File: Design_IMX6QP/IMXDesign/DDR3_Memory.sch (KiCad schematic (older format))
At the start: 0 parts

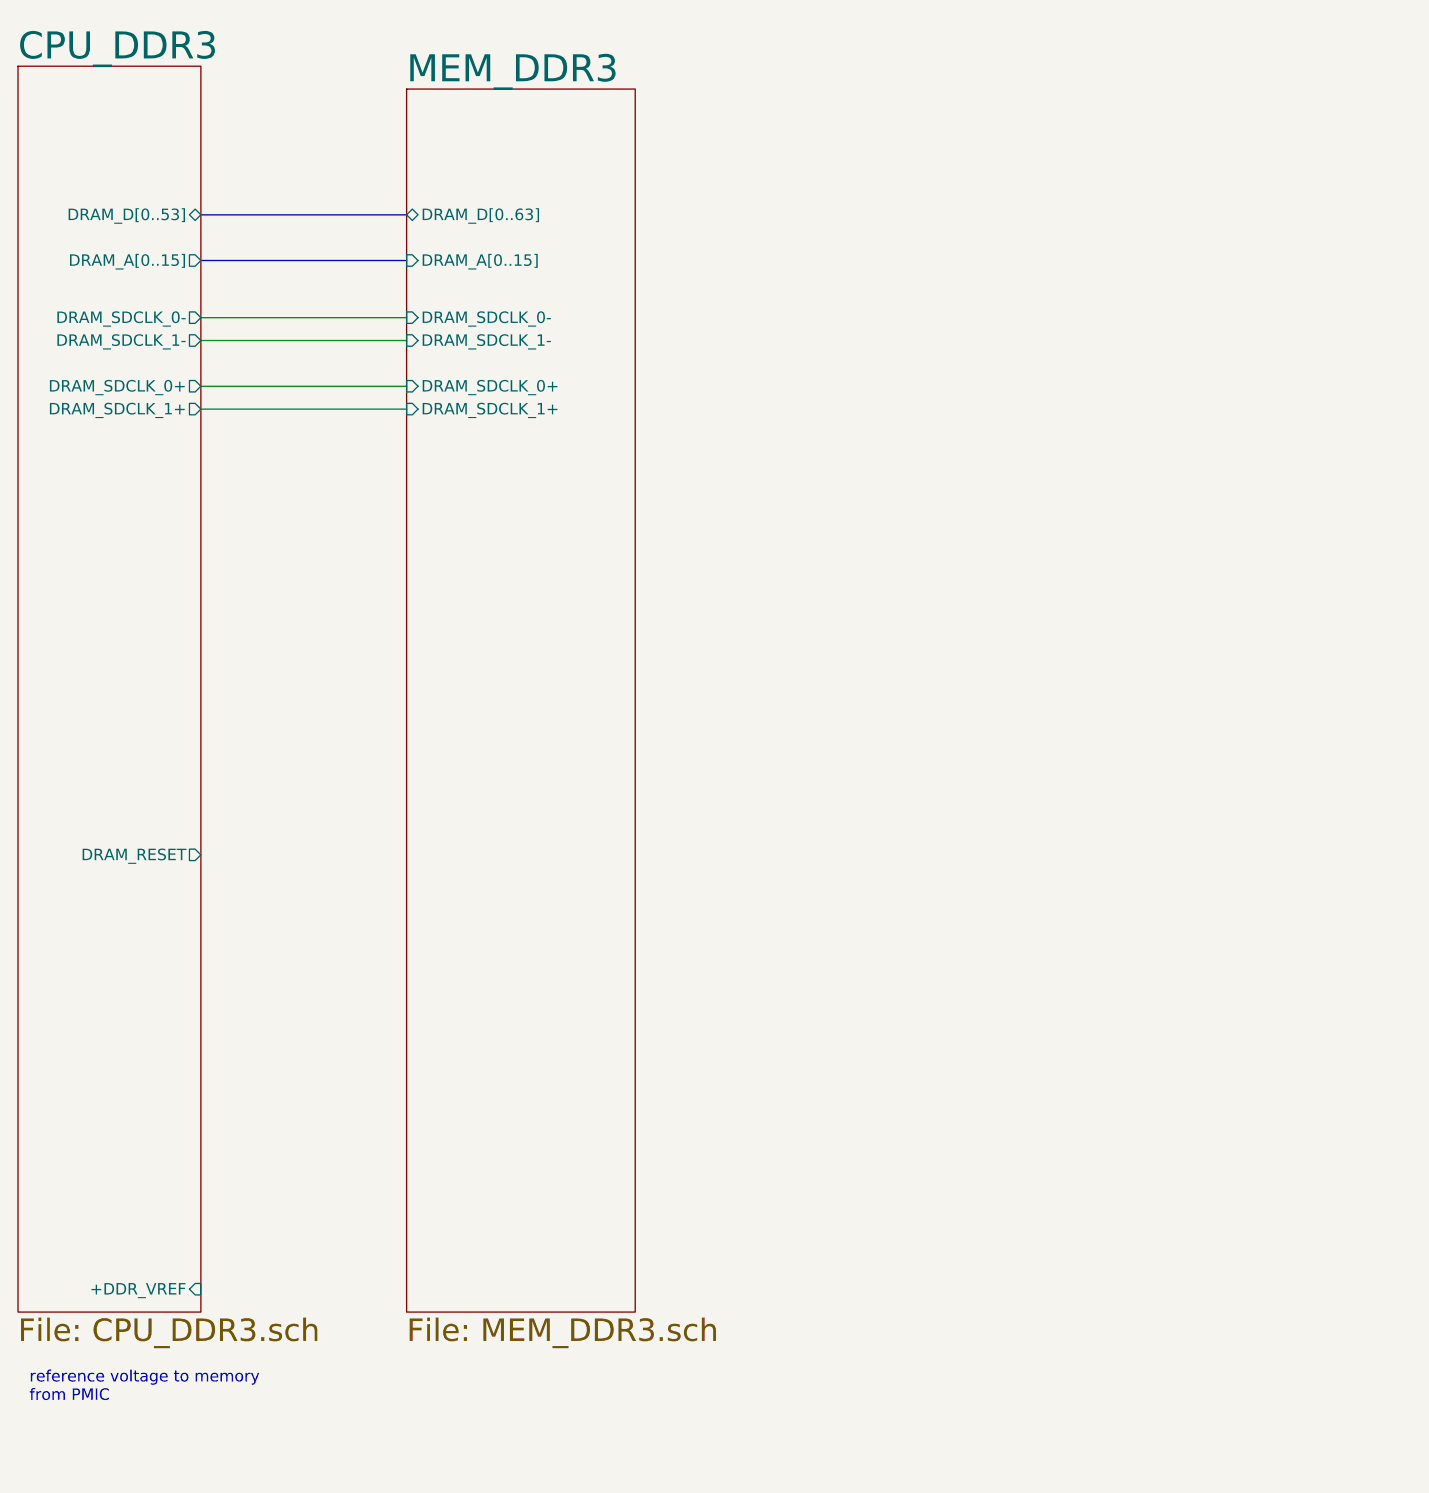
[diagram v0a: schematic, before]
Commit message: Update IMX6QP and IMX8MQ
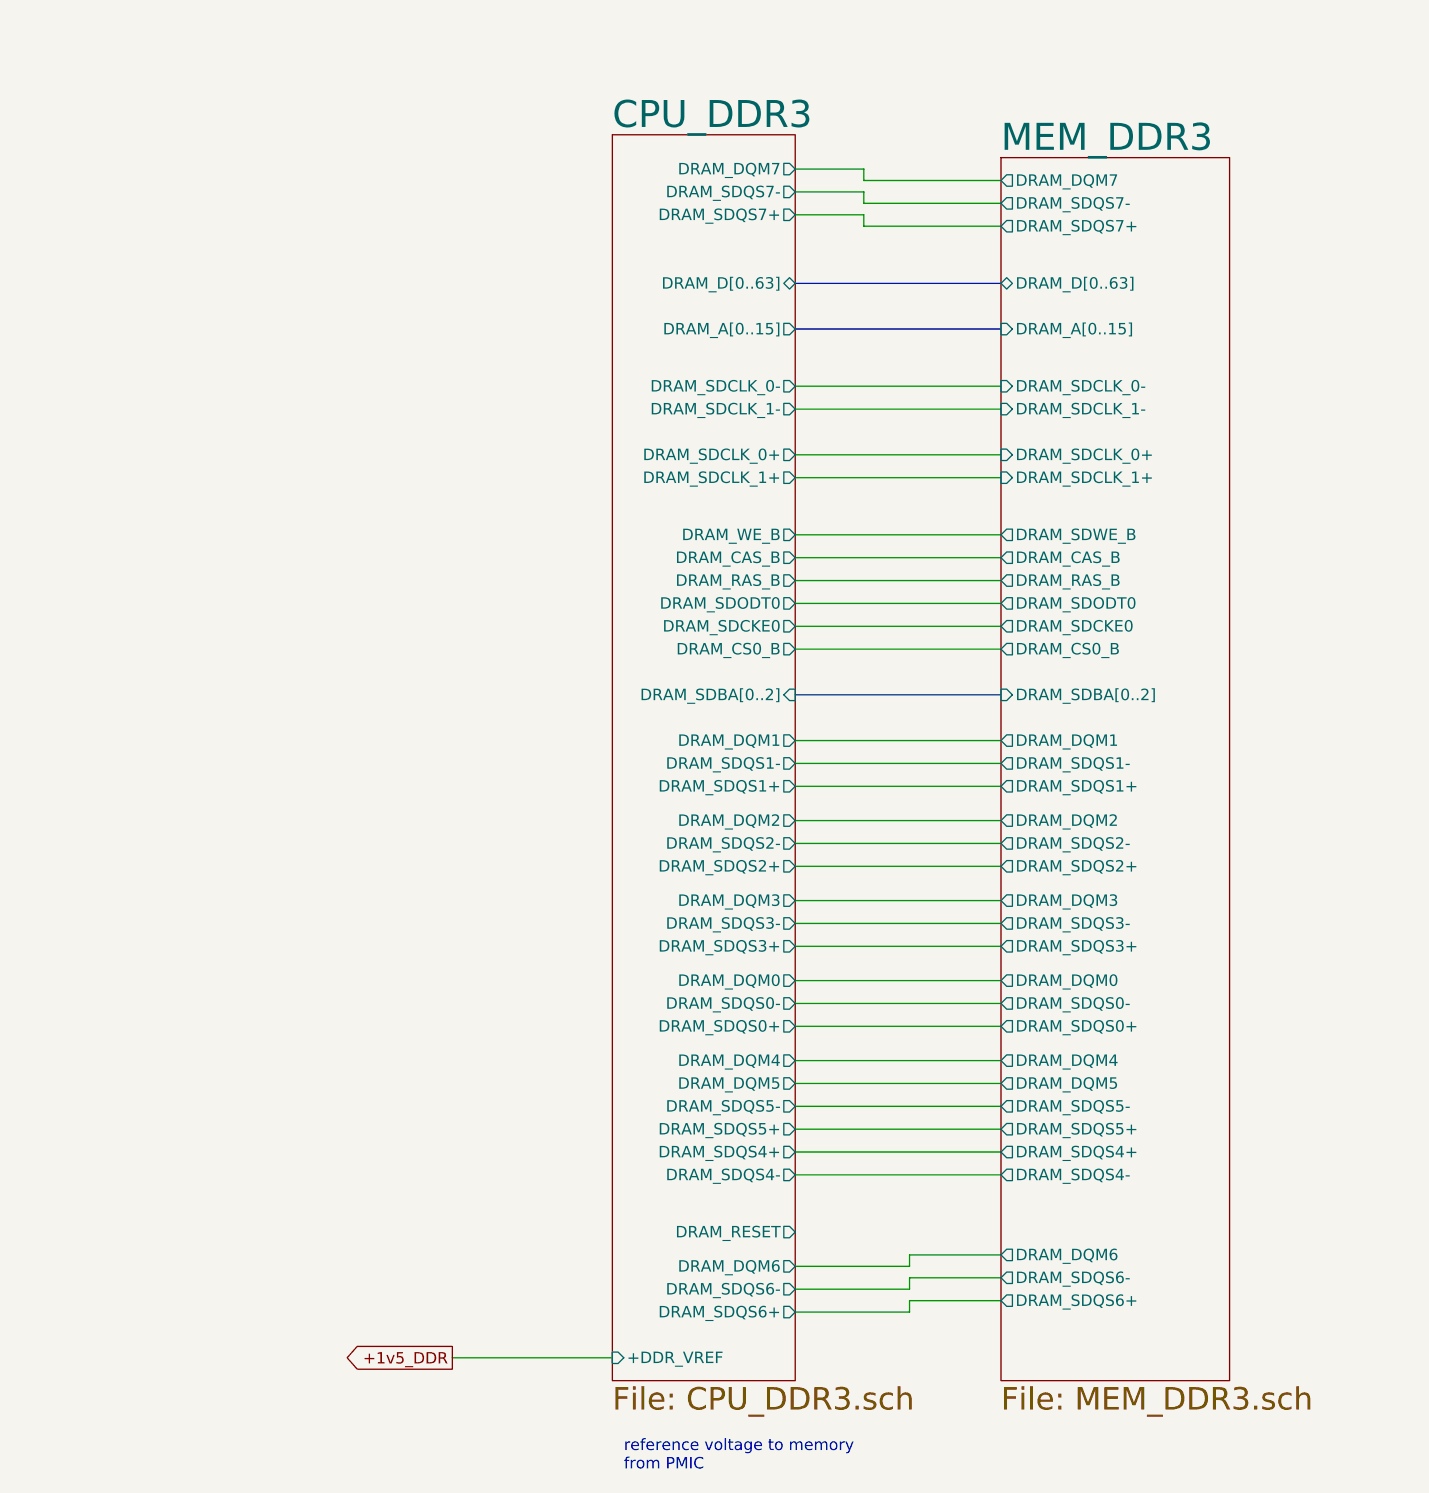
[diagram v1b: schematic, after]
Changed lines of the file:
@@
 $Descr A4 11693 8268
 encoding utf-8
-Sheet 2 12
+Sheet 2 17
 Title ""
 Date ""
@@
 Comment4 ""
 $EndDescr
-Text Notes 1000 6600 0    50   ~ 0
+Text Notes 3600 6900 0    50   ~ 0
 reference voltage to memory\nfrom PMIC
+Wire Wire Line
+	4350 2250 5250 2250
+Wire Wire Line
+	4350 2450 5250 2450
+Wire Wire Line
+	4350 2550 5250 2550
+Text GLabel 2850 6400 0    50   Output ~ 0
++1v5_DDR
+Wire Wire Line
+	4350 2800 5250 2800
+Wire Wire Line
+	5250 2900 4350 2900
+Wire Wire Line
+	4350 3000 5250 3000
+Wire Wire Line
+	5250 3100 4350 3100
+Wire Wire Line
+	4350 3200 5250 3200
+Wire Wire Line
+	4350 3300 5250 3300
 $Sheet
-S 2650 850  1000 5350
+S 5250 1150 1000 5350
 U 632D5505
 F0 "MEM_DDR3" 118
 F1 "MEM_DDR3.sch" 98
-F2 "DRAM_D[0..63]" B L 2650 1400 50
-F3 "DRAM_A[0..15]" I L 2650 1600 50
-F4 "DRAM_SDCLK_0-" I L 2650 1850 50
-F5 "DRAM_SDCLK_1-" I L 2650 1950 50
-F6 "DRAM_SDCLK_0+" I L 2650 2150 50
-F7 "DRAM_SDCLK_1+" I L 2650 2250 50
+F2 "DRAM_D[0..63]" B L 5250 1700 50
+F3 "DRAM_A[0..15]" I L 5250 1900 50
+F4 "DRAM_SDCLK_0-" I L 5250 2150 50
+F5 "DRAM_SDCLK_1-" I L 5250 2250 50
+F6 "DRAM_SDCLK_0+" I L 5250 2450 50
+F7 "DRAM_SDCLK_1+" I L 5250 2550 50
+F8 "DRAM_SDWE_B" O L 5250 2800 50
+F9 "DRAM_CAS_B" O L 5250 2900 50
+F10 "DRAM_RAS_B" O L 5250 3000 50
+F11 "DRAM_SDODT0" O L 5250 3100 50
+F12 "DRAM_SDCKE0" O L 5250 3200 50
+F13 "DRAM_CS0_B" O L 5250 3300 50
+F14 "DRAM_SDBA[0..2]" I L 5250 3500 50
+F15 "DRAM_DQM3" O L 5250 4400 50
+F16 "DRAM_SDQS3-" O L 5250 4500 50
+F17 "DRAM_SDQS3+" O L 5250 4600 50
+F18 "DRAM_DQM2" O L 5250 4050 50
+F19 "DRAM_SDQS2-" O L 5250 4150 50
+F20 "DRAM_SDQS2+" O L 5250 4250 50
+F21 "DRAM_DQM1" O L 5250 3700 50
+F22 "DRAM_SDQS1-" O L 5250 3800 50
+F23 "DRAM_SDQS1+" O L 5250 3900 50
+F24 "DRAM_DQM0" O L 5250 4750 50
+F25 "DRAM_SDQS0-" O L 5250 4850 50
+F26 "DRAM_SDQS0+" O L 5250 4950 50
+F27 "DRAM_DQM4" O L 5250 5100 50
+F28 "DRAM_DQM5" O L 5250 5200 50
+F29 "DRAM_SDQS5-" O L 5250 5300 50
+F30 "DRAM_SDQS5+" O L 5250 5400 50
+F31 "DRAM_SDQS4+" O L 5250 5500 50
+F32 "DRAM_SDQS4-" O L 5250 5600 50
+F33 "DRAM_DQM6" O L 5250 5950 50
+F34 "DRAM_SDQS6-" O L 5250 6050 50
+F35 "DRAM_SDQS6+" O L 5250 6150 50
+F36 "DRAM_DQM7" O L 5250 1250 50
+F37 "DRAM_SDQS7-" O L 5250 1350 50
+F38 "DRAM_SDQS7+" O L 5250 1450 50
 $EndSheet
 Wire Bus Line
-	1750 1400 2650 1400
+	4350 3500 5250 3500
+Wire Wire Line
+	3550 6400 2850 6400
+Wire Wire Line
+	4350 2150 5250 2150
 Wire Bus Line
-	2650 1600 1750 1600
-Wire Wire Line
-	1750 1950 2650 1950
-Wire Wire Line
-	1750 1850 2650 1850
-Wire Wire Line
-	1750 2150 2650 2150
-Wire Wire Line
-	1750 2250 2650 2250
+	5250 1900 4350 1900
+Wire Bus Line
+	4350 1700 5250 1700
 $Sheet
-S 950  750  800  5450
+S 3550 1050 800  5450
 U 63294BDF
 F0 "CPU_DDR3" 118
 F1 "CPU_DDR3.sch" 98
-F2 "DRAM_D[0..53]" B R 1750 1400 50
-F3 "DRAM_A[0..15]" O R 1750 1600 50
-F4 "+DDR_VREF" I R 1750 6100 50
-F5 "DRAM_RESET" O R 1750 4200 50
-F6 "DRAM_SDCLK_0-" O R 1750 1850 50
-F7 "DRAM_SDCLK_1-" O R 1750 1950 50
-F8 "DRAM_SDCLK_0+" O R 1750 2150 50
-F9 "DRAM_SDCLK_1+" O R 1750 2250 50
+F2 "DRAM_D[0..63]" B R 4350 1700 50
+F3 "DRAM_A[0..15]" O R 4350 1900 50
+F4 "+DDR_VREF" I L 3550 6400 50
+F5 "DRAM_RESET" O R 4350 5850 50
+F6 "DRAM_SDCLK_0-" O R 4350 2150 50
+F7 "DRAM_SDCLK_1-" O R 4350 2250 50
+F8 "DRAM_SDCLK_0+" O R 4350 2450 50
+F9 "DRAM_SDCLK_1+" O R 4350 2550 50
+F10 "DRAM_WE_B" O R 4350 2800 50
+F11 "DRAM_CAS_B" O R 4350 2900 50
+F12 "DRAM_RAS_B" O R 4350 3000 50
+F13 "DRAM_SDODT0" O R 4350 3100 50
+F14 "DRAM_SDCKE0" O R 4350 3200 50
+F15 "DRAM_CS0_B" O R 4350 3300 50
+F16 "DRAM_SDBA[0..2]" I R 4350 3500 50
+F17 "DRAM_DQM3" O R 4350 4400 50
+F18 "DRAM_SDQS3-" O R 4350 4500 50
+F19 "DRAM_SDQS3+" O R 4350 4600 50
+F20 "DRAM_DQM2" O R 4350 4050 50
+F21 "DRAM_SDQS2-" O R 4350 4150 50
+F22 "DRAM_SDQS2+" O R 4350 4250 50
+F23 "DRAM_DQM1" O R 4350 3700 50
+F24 "DRAM_SDQS1-" O R 4350 3800 50
+F25 "DRAM_SDQS1+" O R 4350 3900 50
+F26 "DRAM_DQM0" O R 4350 4750 50
+F27 "DRAM_SDQS0-" O R 4350 4850 50
+F28 "DRAM_SDQS0+" O R 4350 4950 50
+F29 "DRAM_DQM4" O R 4350 5100 50
+F30 "DRAM_DQM5" O R 4350 5200 50
+F31 "DRAM_SDQS5-" O R 4350 5300 50
+F32 "DRAM_SDQS5+" O R 4350 5400 50
+F33 "DRAM_SDQS4+" O R 4350 5500 50
+F34 "DRAM_SDQS4-" O R 4350 5600 50
+F35 "DRAM_DQM6" O R 4350 6000 50
+F36 "DRAM_SDQS6-" O R 4350 6100 50
+F37 "DRAM_SDQS6+" O R 4350 6200 50
+F38 "DRAM_DQM7" O R 4350 1200 50
+F39 "DRAM_SDQS7-" O R 4350 1300 50
+F40 "DRAM_SDQS7+" O R 4350 1400 50
 $EndSheet
+Wire Wire Line
+	5250 1250 4650 1250
+Wire Wire Line
+	4650 1250 4650 1200
+Wire Wire Line
+	4650 1200 4350 1200
+Wire Wire Line
+	4350 1300 4650 1300
+Wire Wire Line
+	4650 1300 4650 1350
+Wire Wire Line
+	4650 1350 5250 1350
+Wire Wire Line
+	5250 1450 4650 1450
+Wire Wire Line
+	4650 1450 4650 1400
+Wire Wire Line
+	4650 1400 4350 1400
+Wire Wire Line
+	4350 3700 5250 3700
+Wire Wire Line
+	5250 3800 4350 3800
+Wire Wire Line
+	4350 3900 5250 3900
+Wire Wire Line
+	4350 4050 5250 4050
+Wire Wire Line
+	5250 4150 4350 4150
+Wire Wire Line
+	4350 4250 5250 4250
+Wire Wire Line
+	5250 4400 4350 4400
+Wire Wire Line
+	4350 4500 5250 4500
+Wire Wire Line
+	5250 4600 4350 4600
+Wire Wire Line
+	4350 4750 5250 4750
+Wire Wire Line
+	5250 4850 4350 4850
+Wire Wire Line
+	4350 4950 5250 4950
+Wire Wire Line
+	5250 5100 4350 5100
+Wire Wire Line
+	4350 5200 5250 5200
+Wire Wire Line
+	5250 5300 4350 5300
+Wire Wire Line
+	4350 5400 5250 5400
+Wire Wire Line
+	5250 5500 4350 5500
+Wire Wire Line
+	4350 5600 5250 5600
+Wire Wire Line
+	4350 6000 4850 6000
+Wire Wire Line
+	4850 6000 4850 5950
+Wire Wire Line
+	4850 5950 5250 5950
+Wire Wire Line
+	5250 6050 4850 6050
+Wire Wire Line
+	4850 6050 4850 6100
+Wire Wire Line
+	4850 6100 4350 6100
+Wire Wire Line
+	4350 6200 4850 6200
+Wire Wire Line
+	4850 6200 4850 6150
+Wire Wire Line
+	4850 6150 5250 6150
 $EndSCHEMATC
